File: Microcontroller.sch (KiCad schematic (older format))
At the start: 22 parts, among them J3 Conn_02x03_Counter_Clockwise, U3 STM32F446VET6-sternie, U4 OSCILLATOR-sternie

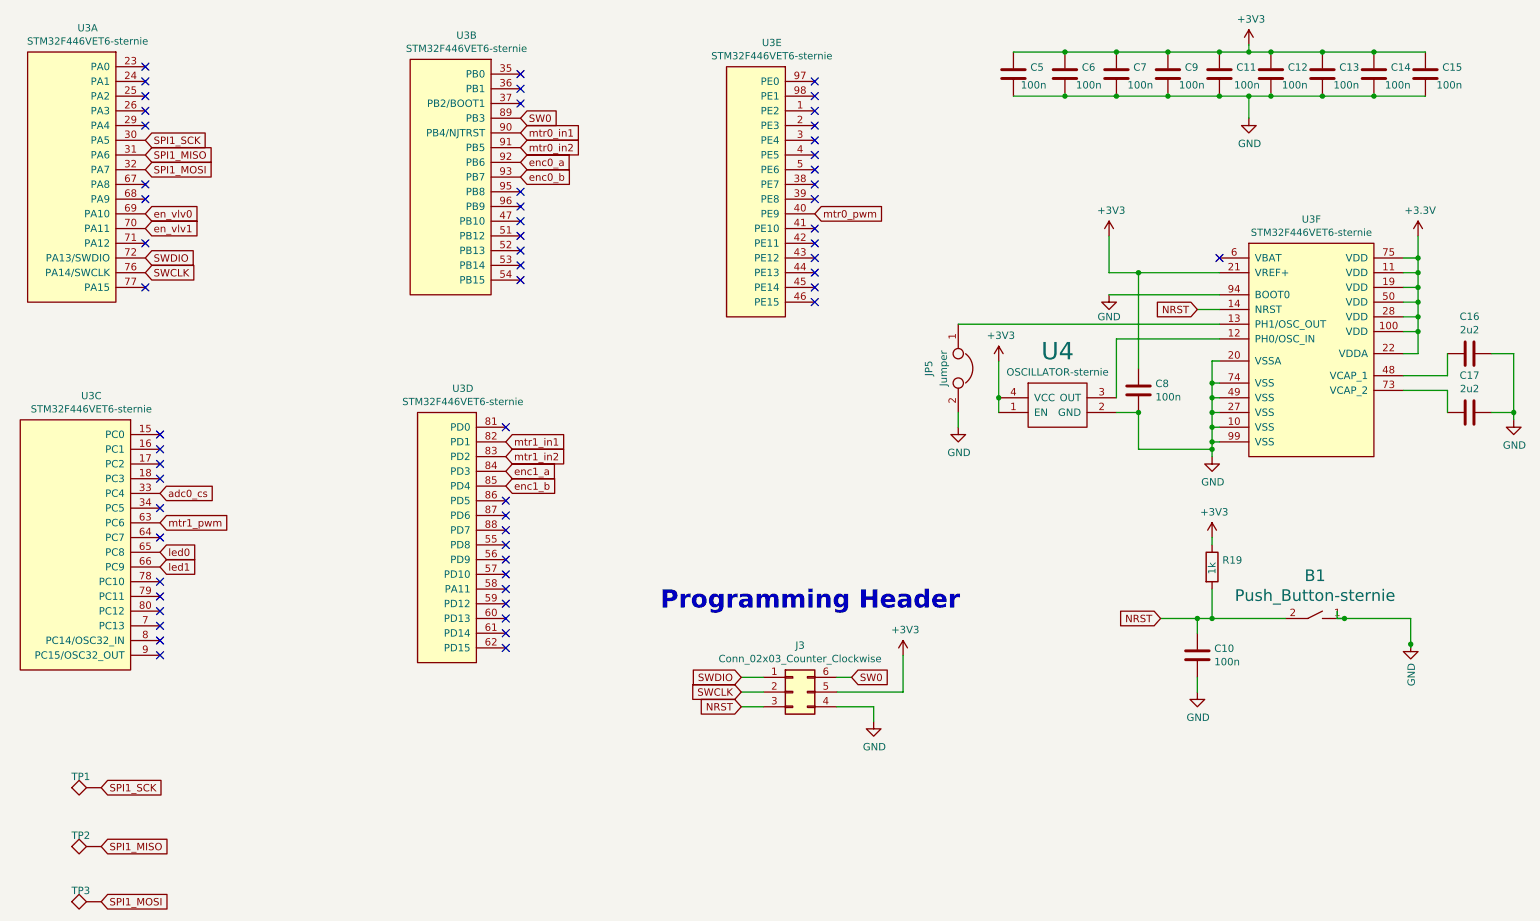
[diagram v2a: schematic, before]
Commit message: fixed up pwm control to hbridge
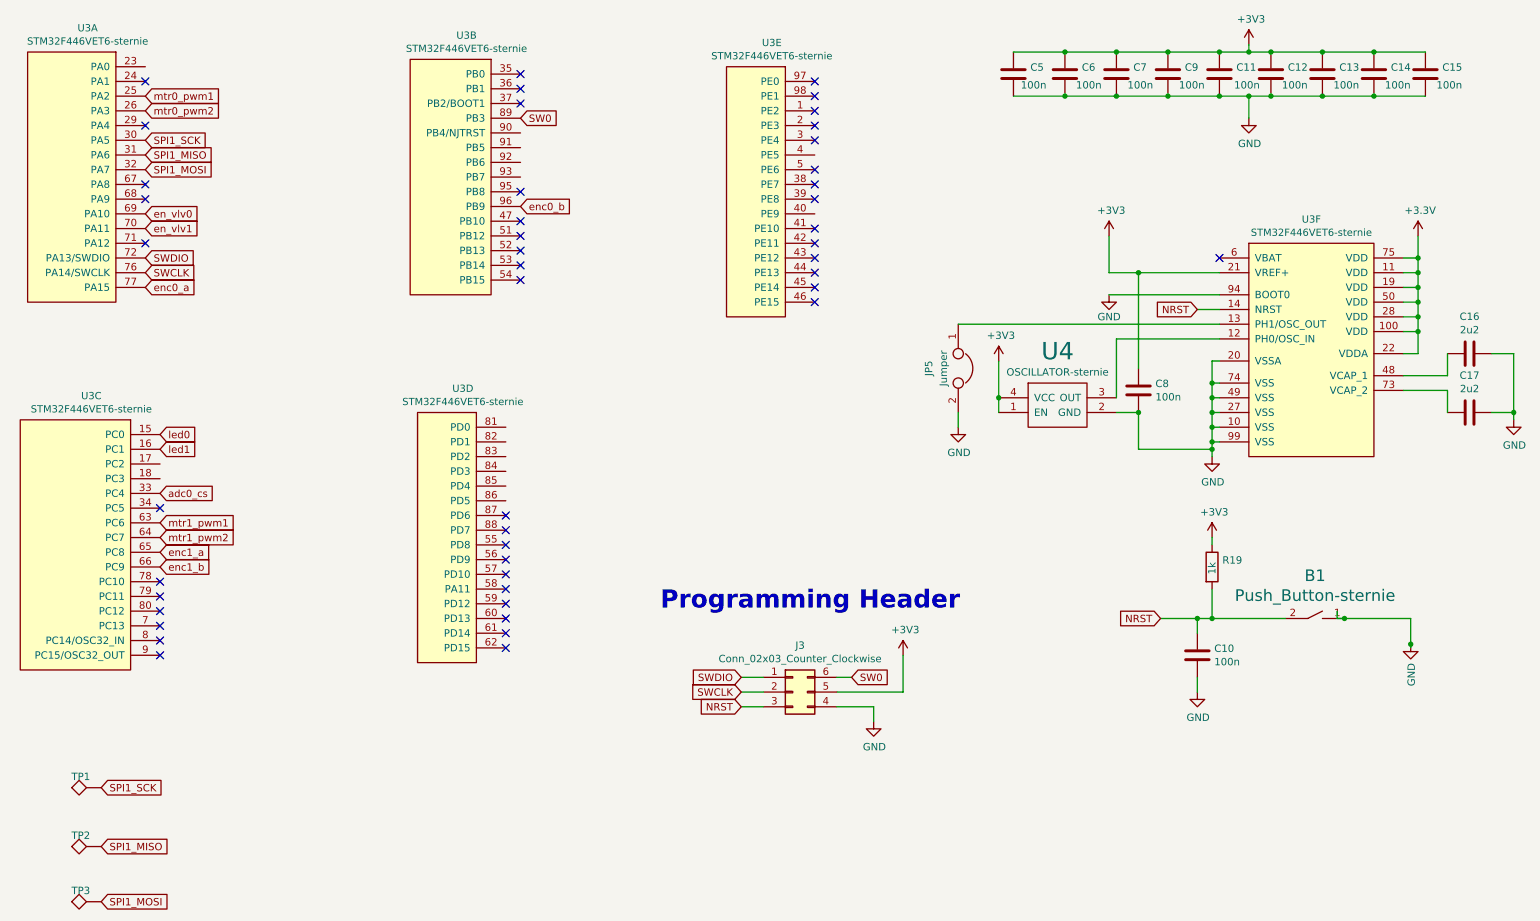
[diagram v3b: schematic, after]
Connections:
- net enc0_a: now also U3.77 (PA15); no longer U3.92 (PB6)
- net enc0_b: now also U3.96 (PB9); no longer U3.93 (PB7)
- net enc1_a: now also U3.65 (PC8); no longer U3.84 (PD3)
- net enc1_b: now also U3.66 (PC9); no longer U3.85 (PD4)
- net led0: now also U3.15 (PC0); no longer U3.65 (PC8)
- net led1: now also U3.16 (PC1); no longer U3.66 (PC9)
- net mtr0_pwm1: now reaches U3.25 (PA2)
- net mtr0_pwm2: now reaches U3.26 (PA3)
- net mtr1_pwm2: now reaches U3.64 (PC7)
- net mtr0_in1: no longer names the net of U3.90 (PB4/NJTRST)
- net mtr0_in2: no longer names the net of U3.91 (PB5)
- net mtr0_pwm: no longer names the net of U3.40 (PE9)
- net mtr1_in1: no longer names the net of U3.82 (PD1)
- net mtr1_in2: no longer names the net of U3.83 (PD2)
- net mtr1_pwm renamed mtr1_pwm1
- no-connect marks 59 -> 46
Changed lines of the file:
@@
 Text GLabel 1750 2400 2    50   Input ~ 0
 en_vlv1
-Text GLabel 4300 1750 2    50   Input ~ 0
-mtr0_in1
-Text GLabel 4300 1850 2    50   Input ~ 0
-mtr0_in2
+Text GLabel 1750 1500 2    50   Input ~ 0
+mtr0_pwm1
+Text GLabel 1750 1600 2    50   Input ~ 0
+mtr0_pwm2
 Text Notes 5250 5000 0    123  ~ 25
 Programming Header\n
@@
 	1    0    0    -1
 $EndComp
-Text GLabel 4200 3850 2    50   Input ~ 0
-mtr1_in1
-Text GLabel 4200 3950 2    50   Input ~ 0
-mtr1_in2
-Text GLabel 4300 1950 2    50   Input ~ 0
+Text GLabel 1850 4400 2    50   Input ~ 0
+mtr1_pwm1
+Text GLabel 1850 4500 2    50   Input ~ 0
+mtr1_pwm2
+Text GLabel 1750 2800 2    50   Input ~ 0
 enc0_a
-Text GLabel 4300 2050 2    50   Input ~ 0
+Text GLabel 4300 2250 2    50   Input ~ 0
 enc0_b
-Text GLabel 4200 4050 2    50   Input ~ 0
+Text GLabel 1850 4600 2    50   Input ~ 0
 enc1_a
-Text GLabel 4200 4150 2    50   Input ~ 0
+Text GLabel 1850 4700 2    50   Input ~ 0
 enc1_b
-Text GLabel 1850 4400 2    50   Input ~ 0
-mtr1_pwm
-Text GLabel 6300 2300 2    50   Input ~ 0
-mtr0_pwm
-Text GLabel 1850 4600 2    50   Input ~ 0
+Text GLabel 1850 3800 2    50   Input ~ 0
 led0
-Text GLabel 1850 4700 2    50   Input ~ 0
+Text GLabel 1850 3900 2    50   Input ~ 0
 led1
 Text GLabel 1450 6200 2    50   Input ~ 0
@@
 Text GLabel 1850 4200 2    49   Input ~ 0
 adc0_cs
-NoConn ~ 1750 1300
 NoConn ~ 1750 1400
-NoConn ~ 1750 1500
-NoConn ~ 1750 1600
 NoConn ~ 1750 1700
 NoConn ~ 1750 2100
 NoConn ~ 1750 2200
 NoConn ~ 1750 2500
-NoConn ~ 1750 2800
-NoConn ~ 1850 3800
-NoConn ~ 1850 3900
-NoConn ~ 1850 4000
-NoConn ~ 1850 4100
 NoConn ~ 1850 4300
-NoConn ~ 1850 4500
 NoConn ~ 1850 4800
 NoConn ~ 1850 4900
@@
 NoConn ~ 4300 1550
 NoConn ~ 4300 2150
-NoConn ~ 4300 2250
 NoConn ~ 4300 2350
 NoConn ~ 4300 2450
@@
 NoConn ~ 4200 4450
 NoConn ~ 4200 4350
-NoConn ~ 4200 4250
-NoConn ~ 4200 3750
 NoConn ~ 6300 1400
 NoConn ~ 6300 1500
@@
 NoConn ~ 6300 1700
 NoConn ~ 6300 1800
-NoConn ~ 6300 1900
 NoConn ~ 6300 2000
 NoConn ~ 6300 2100

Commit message: Motor Channel Cleanup
Removed some leftover labels in the motor channel after removal of the AND gate. Renumbering.
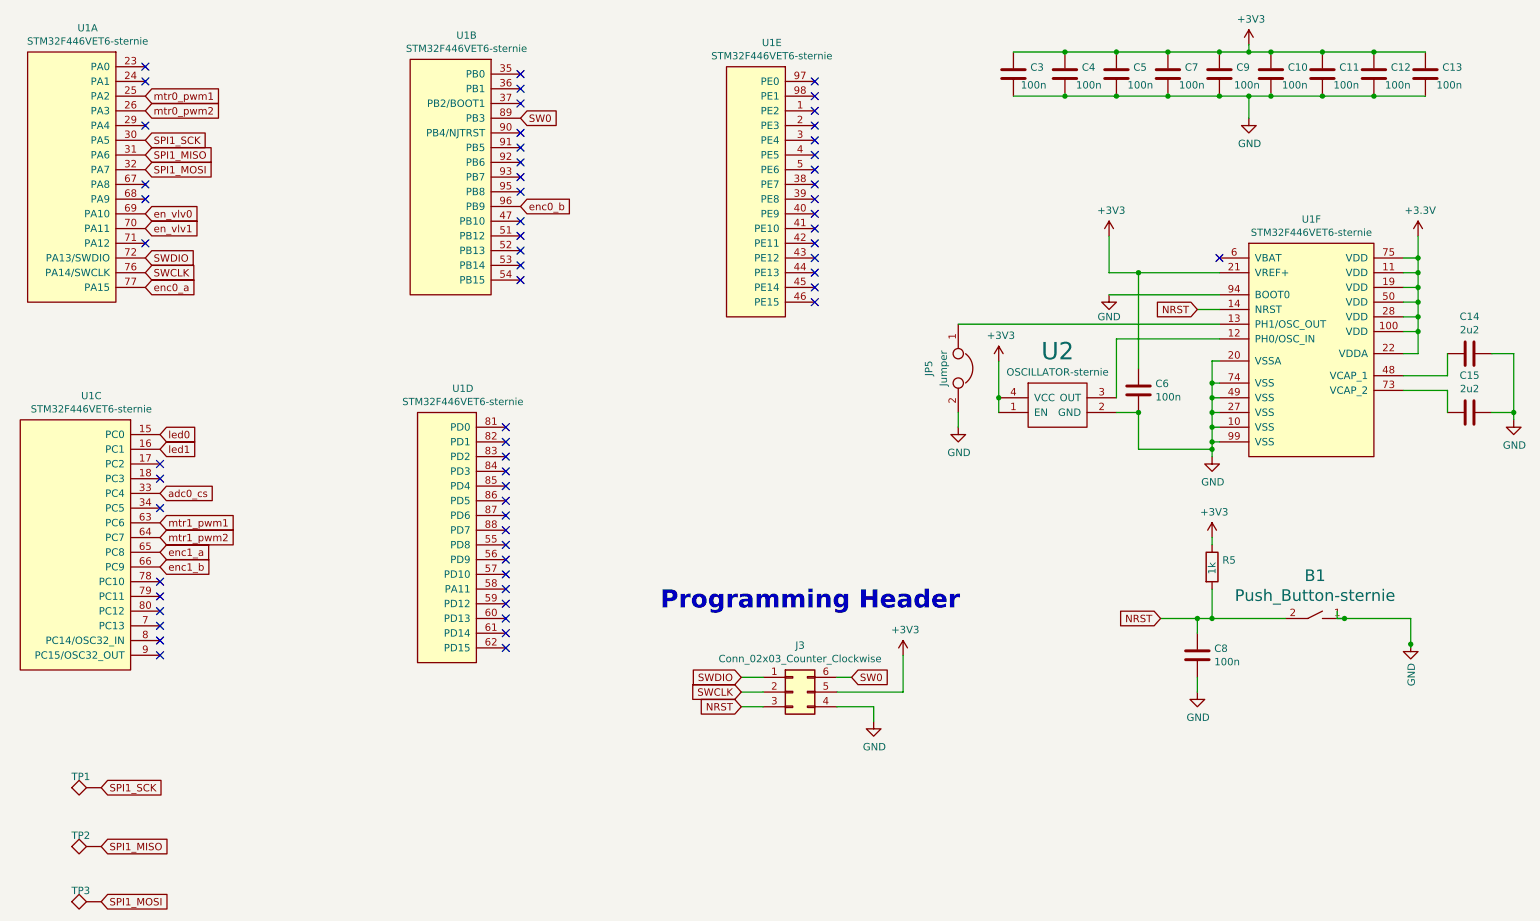
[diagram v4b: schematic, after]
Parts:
- renumbered C12 to C10, C13 to C11, C14 to C12, C15 to C13, C16 to C14, C17 to C15, C5 to C3, C6 to C4, C7 to C5, C8 to C6, C9 to C7, C10 to C8, C11 to C9, R19 to R5, U3 to U1, U4 to U2
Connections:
- no-connect marks 46 -> 61
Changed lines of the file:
@@
 $EndDescr
 $Comp
-L bangbang_rev1-rescue:STM32F446VET6-sternie-engine_controller_series3-rescue U3
+L bangbang_rev1-rescue:STM32F446VET6-sternie-engine_controller_series3-rescue U1
 U 1 1 5E534371
 P 1750 1300
-F 0 "U3" H 1358 1563 49  0000 C CNN
+F 0 "U1" H 1358 1563 49  0000 C CNN
 F 1 "STM32F446VET6-sternie" H 1358 1473 49  0000 C CNN
 F 2 "" H 900 350 49  0001 C CNN
@@
 $EndComp
 $Comp
-L bangbang_rev1-rescue:STM32F446VET6-sternie-engine_controller_series3-rescue U3
+L bangbang_rev1-rescue:STM32F446VET6-sternie-engine_controller_series3-rescue U1
 U 2 1 5E53758A
 P 4300 1350
-F 0 "U3" H 3933 1613 49  0000 C CNN
+F 0 "U1" H 3933 1613 49  0000 C CNN
 F 1 "STM32F446VET6-sternie" H 3933 1523 49  0000 C CNN
 F 2 "" H 3450 400 49  0001 C CNN
@@
 $EndComp
 $Comp
-L bangbang_rev1-rescue:STM32F446VET6-sternie-engine_controller_series3-rescue U3
+L bangbang_rev1-rescue:STM32F446VET6-sternie-engine_controller_series3-rescue U1
 U 3 1 5E53B3C0
 P 1850 3800
-F 0 "U3" H 1383 4063 49  0000 C CNN
+F 0 "U1" H 1383 4063 49  0000 C CNN
 F 1 "STM32F446VET6-sternie" H 1383 3973 49  0000 C CNN
 F 2 "" H 1000 2850 49  0001 C CNN
@@
 $EndComp
 $Comp
-L bangbang_rev1-rescue:STM32F446VET6-sternie-engine_controller_series3-rescue U3
+L bangbang_rev1-rescue:STM32F446VET6-sternie-engine_controller_series3-rescue U1
 U 4 1 5E53EB96
 P 4200 3750
-F 0 "U3" H 3908 4013 49  0000 C CNN
+F 0 "U1" H 3908 4013 49  0000 C CNN
 F 1 "STM32F446VET6-sternie" H 3908 3923 49  0000 C CNN
 F 2 "" H 3350 2800 49  0001 C CNN
@@
 $EndComp
 $Comp
-L bangbang_rev1-rescue:STM32F446VET6-sternie-engine_controller_series3-rescue U3
+L bangbang_rev1-rescue:STM32F446VET6-sternie-engine_controller_series3-rescue U1
 U 5 1 5E54171C
 P 6300 1400
-F 0 "U3" H 6008 1663 49  0000 C CNN
+F 0 "U1" H 6008 1663 49  0000 C CNN
 F 1 "STM32F446VET6-sternie" H 6008 1573 49  0000 C CNN
 F 2 "" H 5450 450 49  0001 C CNN
@@
 	6700 5650 6700 5750
 $Comp
-L power:+3V3 #PWR035
+L power:+3V3 #PWR09
 U 1 1 5E5398EA
 P 6900 5300
-F 0 "#PWR035" H 6900 5150 50  0001 C CNN
+F 0 "#PWR09" H 6900 5150 50  0001 C CNN
 F 1 "+3V3" H 6915 5473 50  0000 C CNN
 F 2 "" H 6900 5300 50  0001 C CNN
@@
 $EndComp
 $Comp
-L power:GND #PWR034
+L power:GND #PWR08
 U 1 1 5E53A4AC
 P 6700 5750
-F 0 "#PWR034" H 6700 5500 50  0001 C CNN
+F 0 "#PWR08" H 6700 5500 50  0001 C CNN
 F 1 "GND" H 6705 5577 50  0000 C CNN
 F 2 "" H 6700 5750 50  0001 C CNN
@@
 $EndComp
 $Comp
-L bangbang_rev1-rescue:STM32F446VET6-sternie-engine_controller_series3-rescue U3
+L bangbang_rev1-rescue:STM32F446VET6-sternie-engine_controller_series3-rescue U1
 U 6 1 5E53BC0E
 P 9700 3050
-F 0 "U3" H 9675 3763 49  0000 C CNN
+F 0 "U1" H 9675 3763 49  0000 C CNN
 F 1 "STM32F446VET6-sternie" H 9675 3673 49  0000 C CNN
 F 2 "" H 8850 2100 49  0001 C CNN
@@
 NRST
 $Comp
-L bangbang_rev1-rescue:OSCILLATOR-sternie-engine_controller_series3-rescue U4
+L bangbang_rev1-rescue:OSCILLATOR-sternie-engine_controller_series3-rescue U2
 U 1 1 5E54009F
 P 7950 3600
-F 0 "U4" H 7950 3966 118 0000 C CNN
+F 0 "U2" H 7950 3966 118 0000 C CNN
 F 1 "OSCILLATOR-sternie" H 7950 3824 50  0000 C CNN
 F 2 "" H 7950 3600 118 0001 C CNN
@@
 Connection ~ 10400 2600
 $Comp
-L power:+3.3V #PWR046
+L power:+3.3V #PWR020
 U 1 1 5E5CF66B
 P 10400 2450
-F 0 "#PWR046" H 10400 2300 50  0001 C CNN
+F 0 "#PWR020" H 10400 2300 50  0001 C CNN
 F 1 "+3.3V" H 10415 2623 50  0000 C CNN
 F 2 "" H 10400 2450 50  0001 C CNN
@@
 $EndComp
 $Comp
-L Device:C C16
+L Device:C C14
 U 1 1 5E5D5552
 P 10750 3250
-F 0 "C16" V 10498 3250 50  0000 C CNN
+F 0 "C14" V 10498 3250 50  0000 C CNN
 F 1 "2u2" V 10589 3250 50  0000 C CNN
 F 2 "" H 10788 3100 50  0001 C CNN
@@
 $EndComp
 $Comp
-L Device:C C17
+L Device:C C15
 U 1 1 5E5D60AC
 P 10750 3650
-F 0 "C17" V 10498 3650 50  0000 C CNN
+F 0 "C15" V 10498 3650 50  0000 C CNN
 F 1 "2u2" V 10589 3650 50  0000 C CNN
 F 2 "" H 10788 3500 50  0001 C CNN
@@
 	11050 3650 11050 3700
 $Comp
-L power:GND #PWR047
+L power:GND #PWR021
 U 1 1 5E5DCF31
 P 11050 3700
-F 0 "#PWR047" H 11050 3450 50  0001 C CNN
+F 0 "#PWR021" H 11050 3450 50  0001 C CNN
 F 1 "GND" H 11055 3527 50  0000 C CNN
 F 2 "" H 11050 3700 50  0001 C CNN
@@
 $EndComp
 $Comp
-L Device:C C8
+L Device:C C6
 U 1 1 5E5E2036
 P 8500 3500
-F 0 "C8" H 8615 3546 50  0000 L CNN
+F 0 "C6" H 8615 3546 50  0000 L CNN
 F 1 "100n" H 8615 3455 50  0000 L CNN
 F 2 "" H 8538 3350 50  0001 C CNN
@@
 	9000 3900 9000 3950
 $Comp
-L power:GND #PWR041
+L power:GND #PWR015
 U 1 1 5E5EC06E
 P 9000 3950
-F 0 "#PWR041" H 9000 3700 50  0001 C CNN
+F 0 "#PWR015" H 9000 3700 50  0001 C CNN
 F 1 "GND" H 9005 3777 50  0000 C CNN
 F 2 "" H 9000 3950 50  0001 C CNN
@@
 	7550 3550 7550 3300
 $Comp
-L power:+3V3 #PWR036
+L power:+3V3 #PWR011
 U 1 1 5E5FF2C5
 P 7550 3300
-F 0 "#PWR036" H 7550 3150 50  0001 C CNN
+F 0 "#PWR011" H 7550 3150 50  0001 C CNN
 F 1 "+3V3" H 7565 3473 50  0000 C CNN
 F 2 "" H 7550 3300 50  0001 C CNN
@@
 $EndComp
 $Comp
-L power:+3V3 #PWR039
+L power:+3V3 #PWR012
 U 1 1 5E604922
 P 8300 2450
-F 0 "#PWR039" H 8300 2300 50  0001 C CNN
+F 0 "#PWR012" H 8300 2300 50  0001 C CNN
 F 1 "+3V3" H 8315 2623 50  0000 C CNN
 F 2 "" H 8300 2450 50  0001 C CNN
@@
 	7275 3650 7275 3750
 $Comp
-L power:GND #PWR037
+L power:GND #PWR010
 U 1 1 5E6156CF
 P 7275 3750
-F 0 "#PWR037" H 7275 3500 50  0001 C CNN
+F 0 "#PWR010" H 7275 3500 50  0001 C CNN
 F 1 "GND" H 7280 3577 50  0000 C CNN
 F 2 "" H 7275 3750 50  0001 C CNN
@@
 $EndComp
 $Comp
-L Device:C C6
+L Device:C C4
 U 1 1 5E616E7B
 P 8000 1350
-F 0 "C6" H 8115 1396 50  0000 L CNN
+F 0 "C4" H 8115 1396 50  0000 L CNN
 F 1 "100n" H 8075 1275 50  0000 L CNN
 F 2 "" H 8038 1200 50  0001 C CNN
@@
 $EndComp
 $Comp
-L Device:C C7
+L Device:C C5
 U 1 1 5E617F70
 P 8350 1350
-F 0 "C7" H 8465 1396 50  0000 L CNN
+F 0 "C5" H 8465 1396 50  0000 L CNN
 F 1 "100n" H 8425 1275 50  0000 L CNN
 F 2 "" H 8388 1200 50  0001 C CNN
@@
 $EndComp
 $Comp
-L Device:C C9
+L Device:C C7
 U 1 1 5E61C3E9
 P 8700 1350
-F 0 "C9" H 8815 1396 50  0000 L CNN
+F 0 "C7" H 8815 1396 50  0000 L CNN
 F 1 "100n" H 8775 1275 50  0000 L CNN
 F 2 "" H 8738 1200 50  0001 C CNN
@@
 $EndComp
 $Comp
-L Device:C C11
+L Device:C C9
 U 1 1 5E61C3EF
 P 9050 1350
-F 0 "C11" H 9165 1396 50  0000 L CNN
+F 0 "C9" H 9165 1396 50  0000 L CNN
 F 1 "100n" H 9150 1275 50  0000 L CNN
 F 2 "" H 9088 1200 50  0001 C CNN
@@
 $EndComp
 $Comp
-L Device:C C12
+L Device:C C10
 U 1 1 5E61ECE7
 P 9400 1350
-F 0 "C12" H 9515 1396 50  0000 L CNN
+F 0 "C10" H 9515 1396 50  0000 L CNN
 F 1 "100n" H 9475 1275 50  0000 L CNN
 F 2 "" H 9438 1200 50  0001 C CNN
@@
 $EndComp
 $Comp
-L Device:C C13
+L Device:C C11
 U 1 1 5E61ECED
 P 9750 1350
-F 0 "C13" H 9865 1396 50  0000 L CNN
+F 0 "C11" H 9865 1396 50  0000 L CNN
 F 1 "100n" H 9825 1275 50  0000 L CNN
 F 2 "" H 9788 1200 50  0001 C CNN
@@
 $EndComp
 $Comp
-L Device:C C14
+L Device:C C12
 U 1 1 5E620F83
 P 10100 1350
-F 0 "C14" H 10215 1396 50  0000 L CNN
+F 0 "C12" H 10215 1396 50  0000 L CNN
 F 1 "100n" H 10175 1275 50  0000 L CNN
 F 2 "" H 10138 1200 50  0001 C CNN
@@
 $EndComp
 $Comp
-L Device:C C15
+L Device:C C13
 U 1 1 5E620F89
 P 10450 1350
-F 0 "C15" H 10565 1396 50  0000 L CNN
+F 0 "C13" H 10565 1396 50  0000 L CNN
 F 1 "100n" H 10525 1275 50  0000 L CNN
 F 2 "" H 10488 1200 50  0001 C CNN
@@
 $EndComp
 $Comp
-L Device:C C5
+L Device:C C3
 U 1 1 5E624C8A
 P 7650 1350
-F 0 "C5" H 7765 1396 50  0000 L CNN
+F 0 "C3" H 7765 1396 50  0000 L CNN
 F 1 "100n" H 7700 1275 50  0000 L CNN
 F 2 "" H 7688 1200 50  0001 C CNN
@@
 	9250 1500 9050 1500
 $Comp
-L power:GND #PWR044
+L power:GND #PWR018
 U 1 1 5E630D54
 P 9250 1650
-F 0 "#PWR044" H 9250 1400 50  0001 C CNN
+F 0 "#PWR018" H 9250 1400 50  0001 C CNN
 F 1 "GND" H 9255 1477 50  0000 C CNN
 F 2 "" H 9250 1650 50  0001 C CNN
@@
 	9250 1200 9400 1200
 $Comp
-L power:+3V3 #PWR043
+L power:+3V3 #PWR017
 U 1 1 5E6389E3
 P 9250 1150
-F 0 "#PWR043" H 9250 1000 50  0001 C CNN
+F 0 "#PWR017" H 9250 1000 50  0001 C CNN
 F 1 "+3V3" H 9265 1323 50  0000 C CNN
 F 2 "" H 9250 1150 50  0001 C CNN
@@
 	8650 5050 8900 5050
 $Comp
-L Device:C C10
+L Device:C C8
 U 1 1 5E65A900
 P 8900 5300
-F 0 "C10" H 9015 5346 50  0000 L CNN
+F 0 "C8" H 9015 5346 50  0000 L CNN
 F 1 "100n" H 9015 5255 50  0000 L CNN
 F 2 "" H 8938 5150 50  0001 C CNN
@@
 $EndComp
 $Comp
-L Device:R R19
+L Device:R R5
 U 1 1 5E65BE21
 P 9000 4700
-F 0 "R19" H 9070 4746 50  0000 L CNN
+F 0 "R5" H 9070 4746 50  0000 L CNN
 F 1 "1k" V 9000 4650 50  0000 L CNN
 F 2 "" V 8930 4700 50  0001 C CNN
@@
 	9000 4550 9000 4500
 $Comp
-L power:+3V3 #PWR042
+L power:+3V3 #PWR016
 U 1 1 5E6634C3
 P 9000 4500
-F 0 "#PWR042" H 9000 4350 50  0001 C CNN
+F 0 "#PWR016" H 9000 4350 50  0001 C CNN
 F 1 "+3V3" H 9015 4673 50  0000 C CNN
 F 2 "" H 9000 4500 50  0001 C CNN
@@
 	8900 5450 8900 5550
 $Comp
-L power:GND #PWR045
+L power:GND #PWR019
 U 1 1 5E66819F
 P 10350 5225
-F 0 "#PWR045" H 10350 4975 50  0001 C CNN
+F 0 "#PWR019" H 10350 4975 50  0001 C CNN
 F 1 "GND" V 10355 5097 50  0000 R CNN
 F 2 "" H 10350 5225 50  0001 C CNN
@@
 $EndComp
 $Comp
-L power:GND #PWR040
+L power:GND #PWR014
 U 1 1 5E6696F3
 P 8900 5550
-F 0 "#PWR040" H 8900 5300 50  0001 C CNN
+F 0 "#PWR014" H 8900 5300 50  0001 C CNN
 F 1 "GND" H 8905 5377 50  0000 C CNN
 F 2 "" H 8900 5550 50  0001 C CNN
@@
 	7275 3050 9050 3050
 $Comp
-L power:GND #PWR038
+L power:GND #PWR013
 U 1 1 5E604DB8
 P 8300 2850
-F 0 "#PWR038" H 8300 2600 50  0001 C CNN
+F 0 "#PWR013" H 8300 2600 50  0001 C CNN
 F 1 "GND" H 8300 2700 50  0000 C CNN
 F 2 "" H 8300 2850 50  0001 C CNN
@@
 	8300 2850 9050 2850
 NoConn ~ 1850 5000
+NoConn ~ 4200 3750
+NoConn ~ 4200 3850
+NoConn ~ 4200 3950
+NoConn ~ 4200 4050
+NoConn ~ 4200 4150
+NoConn ~ 4200 4250
+NoConn ~ 4300 1750
+NoConn ~ 4300 1850
+NoConn ~ 4300 1950
+NoConn ~ 4300 2050
+NoConn ~ 6300 1900
+NoConn ~ 6300 2300
+NoConn ~ 1750 1300
+NoConn ~ 1850 4000
+NoConn ~ 1850 4100
 $EndSCHEMATC
